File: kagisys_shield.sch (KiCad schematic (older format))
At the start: 1 part, among them J1 Conn1

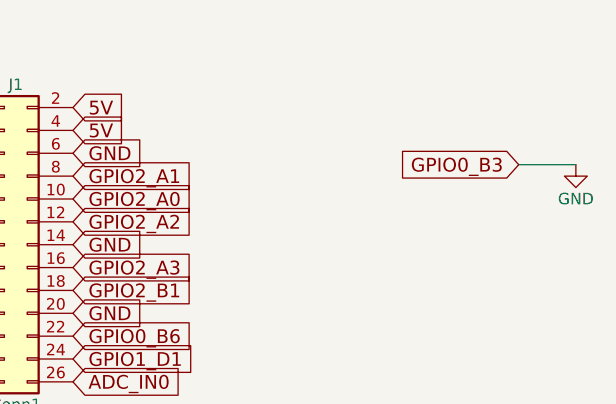
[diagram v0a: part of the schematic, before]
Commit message: add powerflag
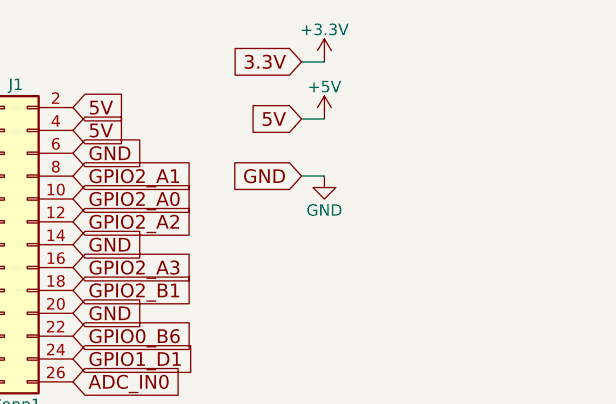
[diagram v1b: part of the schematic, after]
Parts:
- J1: footprint (none) -> Pin_Headers:Pin_Header_Straight_2x13_Pitch2.54mm
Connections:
- net GND: no longer J1.3 (Pin_3)
- net 3.3V renamed +3V3
- net 5V renamed +5V
- new net GPIO0_B3: J1.3 (Pin_3)
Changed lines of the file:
@@
 F 0 "J1" H 1600 2450 50  0000 C CNN
 F 1 "Conn1" H 1600 1050 50  0000 C CNN
-F 2 "" H 1550 1750 50  0001 C CNN
+F 2 "Pin_Headers:Pin_Header_Straight_2x13_Pitch2.54mm" H 1550 1750 50  0001 C CNN
 F 3 "" H 1550 1750 50  0001 C CNN
 	1    1550 1750
@@
 Text GLabel 1850 2350 2    60   Input ~ 0
 ADC_IN0
-Text GLabel 3800 1400 0    60   Input ~ 0
-GPIO0_B3
+Text GLabel 2850 950  0    60   Input ~ 0
+3.3V
 $Comp
-L GND #PWR?
-U 1 1 5D5A52F6
-P 4050 1400
-F 0 "#PWR?" H 4050 1150 50  0001 C CNN
-F 1 "GND" H 4050 1250 50  0000 C CNN
-F 2 "" H 4050 1400 50  0001 C CNN
-F 3 "" H 4050 1400 50  0001 C CNN
-	1    4050 1400
+L +3.3V #PWR?
+U 1 1 5D5A6894
+P 2950 950
+F 0 "#PWR?" H 2950 800 50  0001 C CNN
+F 1 "+3.3V" H 2950 1090 50  0000 C CNN
+F 2 "" H 2950 950 50  0001 C CNN
+F 3 "" H 2950 950 50  0001 C CNN
+	1    2950 950
 	1    0    0    -1
 $EndComp
 Wire Wire Line
-	3800 1400 4050 1400
+	2850 950  2950 950
+Text GLabel 2850 1200 0    60   Input ~ 0
+5V
+$Comp
+L +5V #PWR?
+U 1 1 5D5A68B3
+P 2950 1200
+F 0 "#PWR?" H 2950 1050 50  0001 C CNN
+F 1 "+5V" H 2950 1340 50  0000 C CNN
+F 2 "" H 2950 1200 50  0001 C CNN
+F 3 "" H 2950 1200 50  0001 C CNN
+	1    2950 1200
+	1    0    0    -1
+$EndComp
+Wire Wire Line
+	2850 1200 2950 1200
+Text GLabel 2850 1450 0    60   Input ~ 0
+GND
+$Comp
+L GND #PWR?
+U 1 1 5D5A68D4
+P 2950 1450
+F 0 "#PWR?" H 2950 1200 50  0001 C CNN
+F 1 "GND" H 2950 1300 50  0000 C CNN
+F 2 "" H 2950 1450 50  0001 C CNN
+F 3 "" H 2950 1450 50  0001 C CNN
+	1    2950 1450
+	1    0    0    -1
+$EndComp
+Wire Wire Line
+	2950 1450 2850 1450
 $EndSCHEMATC

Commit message: fix pcb
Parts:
- removed J1: Conn1, Pin_Headers:Pin_Header_Straight_2x13_Pitch2.54mm, symbol Conn_02x13_Odd_Even
- added J1: Conn1, Connector_PinHeader_2.54mm:PinHeader_2x06_P2.54mm_Horizontal, symbol Connector_Generic:Conn_02x06_Odd_Even
- added J2, J6: Conn_01x04_Female, Connector_PinSocket_2.54mm:PinSocket_1x04_P2.54mm_Horizontal, symbol Connector:Conn_01x04_Female
- added J3: Conn_01x03_Female, Connector_PinSocket_2.54mm:PinSocket_1x03_P2.54mm_Horizontal, symbol Connector:Conn_01x03_Female
- added J4, J5: Conn_01x02_Female, Connector_PinSocket_2.54mm:PinSocket_1x02_P2.54mm_Horizontal, symbol Connector:Conn_01x02_Female
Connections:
- net +5V: now also J1.1 (Pin_1), J2.2 (Pin_2), J3.2 (Pin_2), J5.1 (Pin_1), J6.2 (Pin_2)
- net GND: now also J1.11 (Pin_11), J1.3 (Pin_3), J1.8 (Pin_8), J2.1 (Pin_1), J3.1 (Pin_1), J4.2 (Pin_2), J6.1 (Pin_1)
- net GPIO0_B3: now also J1.2 (Pin_2), J2.4 (Pin_4)
- net GPIO0_B4: now also J1.4 (Pin_4), J2.3 (Pin_3)
- net GPIO0_B7: now also J1.10 (Pin_10), J3.3 (Pin_3)
- net GPIO0_C0: now also J1.12 (Pin_12), J4.1 (Pin_1)
- net GPIO2_A0: now also J1.7 (Pin_7), J5.2 (Pin_2)
- net GPIO2_A1: now also J1.5 (Pin_5), J6.3 (Pin_3)
- net GPIO2_A2: now also J1.9 (Pin_9)
- net GPIO2_A5: now also J1.6 (Pin_6), J6.4 (Pin_4)
- no-connect marks 0 -> 1

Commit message: fix pcb
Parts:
- added Q1, Q2: Q_NMOS_GSD, Package_TO_SOT_SMD:SOT-23, symbol Device:Q_NMOS_GSD
- added R1, R2: 10k, Resistor_THT:R_Axial_DIN0309_L9.0mm_D3.2mm_P12.70mm_Horizontal, symbol Device:R
- J1: footprint Connector_PinHeader_2.54mm:PinHeader_2x06_P2.54mm_Horizontal -> Connector_PinHeader_2.54mm:PinHeader_2x07_P2.54mm_Horizontal; symbol Connector_Generic:Conn_02x06_Odd_Even -> Connector_Generic:Conn_02x07_Odd_Even
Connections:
- net +5V: now also J1.3 (Pin_3), R2.1; no longer J5.1 (Pin_1)
- net GND: now also J1.10 (Pin_10), J1.13 (Pin_13), J1.5 (Pin_5), Q2.2 (S), R1.2; no longer J1.11 (Pin_11), J1.3 (Pin_3), J1.8 (Pin_8), J3.1 (Pin_1)
- net GPIO0_B3: now also J1.4 (Pin_4); no longer J1.2 (Pin_2)
- net GPIO0_B4: now also J1.6 (Pin_6); no longer J1.4 (Pin_4)
- net GPIO0_B7: now also J1.12 (Pin_12), Q1.2 (S); no longer J1.10 (Pin_10), J3.3 (Pin_3)
- net GPIO0_C0: now also J1.14 (Pin_14); no longer J1.12 (Pin_12)
- net GPIO2_A0: now also J1.9 (Pin_9); no longer J1.7 (Pin_7)
- net GPIO2_A1: now also J1.7 (Pin_7); no longer J1.5 (Pin_5)
- net GPIO2_A2: now also J1.11 (Pin_11), Q2.1 (G), R1.1; no longer J1.9 (Pin_9)
- net GPIO2_A5: now also J1.8 (Pin_8); no longer J1.6 (Pin_6)
- new net: J3.1 (Pin_1), Q2.3 (D)
- new net: J3.3 (Pin_3), Q1.3 (D), R2.2
- new net 3.3V: J1.2 (Pin_2), J5.1 (Pin_1), Q1.1 (G)
- no-connect marks 1 -> 0
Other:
- moved on the sheet: J2, J3, J4, J5, J6
